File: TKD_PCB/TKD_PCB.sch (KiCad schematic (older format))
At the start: 33 parts, among them U1 ESP32-WROOM-32D

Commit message: Second revision with battery protection circuit attempt
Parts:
- added C? (x3): 0.1uF, symbol Device:C_Small
- added D? (x3): D, symbol Device:D
- added IC?: R5460N208AA-TR-FE, SOT95P280X140-6N, symbol SamacSys_Parts:R5460N233AF-TR-FE
- added Q? (x2): CSD17484F4T, CSD17484F4T, symbol SamacSys_Parts:CSD17484F4T
- added R?: 1k, symbol Device:R
- added R? (x2): 330R, symbol Device:R
- J?: symbol Connector:USB_B_Micro -> TKD_PCB-rescue:USB_B_Micro-Connector
- U?: symbol SamacSys_Parts:1049 -> TKD_PCB-rescue:1049-SamacSys_Parts
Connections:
- net labels added: Batt_1_+, Batt_1_GND, Batt_2_+, Batt_2_GND, Batt_Serie_Connection
- net labels removed: USB_5V_VCC
- wire segments 134 -> 191
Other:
- note added: "Battery Holder for dual 18650"
- note added: "Battery protection circuit"
- note added: "Pad 1 till 6 are screw/attachment pins\nPad 6 = Battery 2 GND\nPad 7 = Battery 1 +\nPad 8 = Battery 2 +\nPad 9 = Battery 1 GND"
- moved on the sheet: C?, D?, R?, SW?, U?

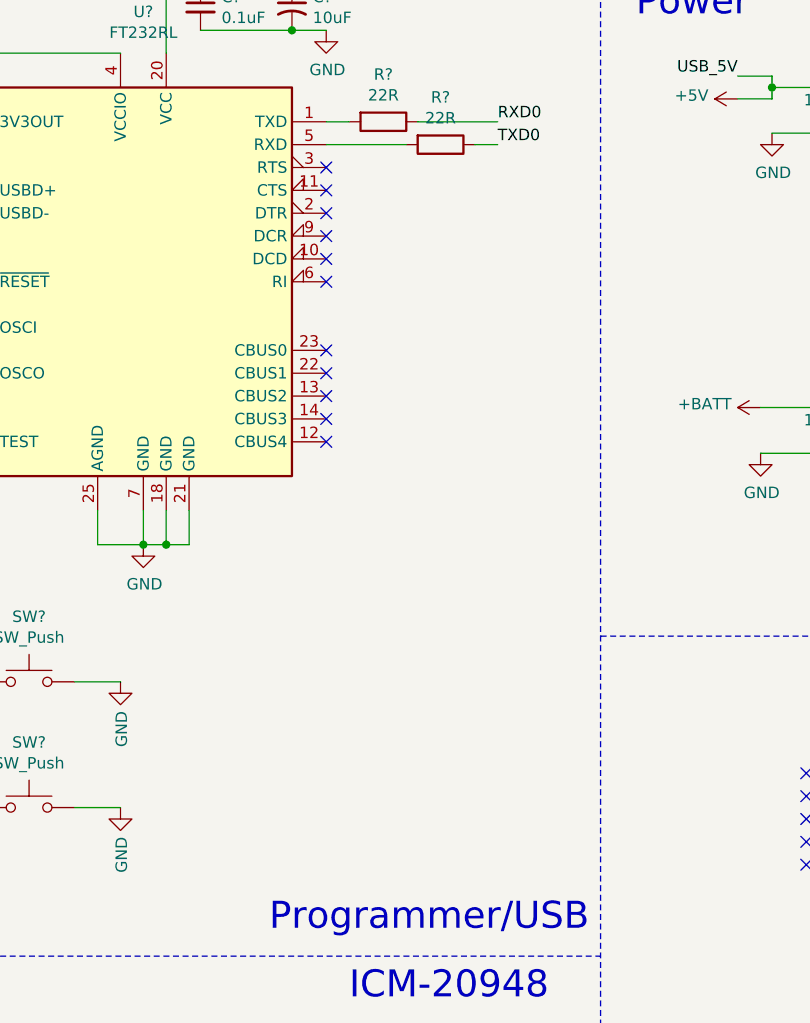
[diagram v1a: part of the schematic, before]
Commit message: Auto programming circuit added
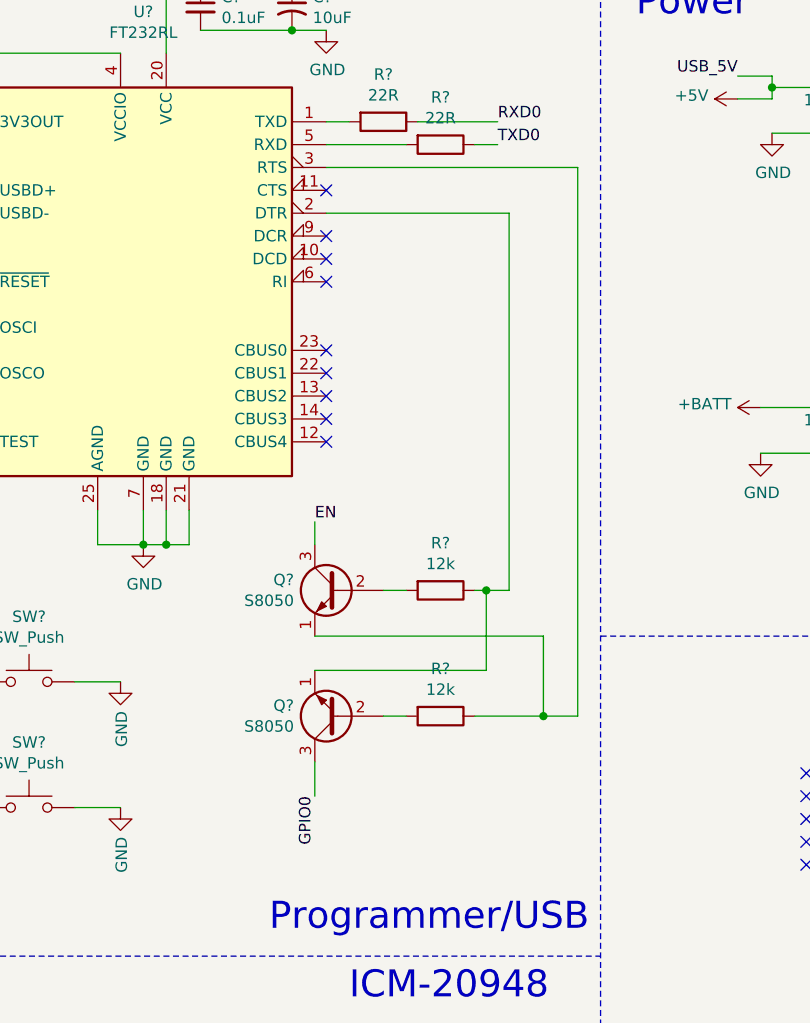
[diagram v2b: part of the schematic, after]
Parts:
- added Q? (x2): S8050, Package_TO_SOT_THT:TO-92_Inline, symbol Transistor_BJT:S8050
- added R? (x2): 12k, symbol Device:R
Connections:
- wire segments 191 -> 207
- no-connect marks 20 -> 18
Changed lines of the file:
@@
 	1    0    0    -1
 $EndComp
-NoConn ~ 6050 1350
 NoConn ~ 6050 1450
-NoConn ~ 6050 1550
 NoConn ~ 6050 1650
 NoConn ~ 6050 1750
@@
 Text Notes 11500 3900 0    50   ~ 0
 Battery protection circuit
+$Comp
+L Transistor_BJT:S8050 Q?
+U 1 1 60276841
+P 6100 3750
+F 0 "Q?" H 6291 3704 50  0000 L CNN
+F 1 "S8050" H 6291 3795 50  0000 L CNN
+F 2 "Package_TO_SOT_THT:TO-92_Inline" H 6300 3675 50  0001 L CIN
+F 3 "http://www.unisonic.com.tw/datasheet/S8050.pdf" H 6100 3750 50  0001 L CNN
+	1    6100 3750
+	-1   0    0    1
+$EndComp
+$Comp
+L Transistor_BJT:S8050 Q?
+U 1 1 602739FF
+P 6100 3200
+F 0 "Q?" H 6291 3246 50  0000 L CNN
+F 1 "S8050" H 6291 3155 50  0000 L CNN
+F 2 "Package_TO_SOT_THT:TO-92_Inline" H 6300 3125 50  0001 L CIN
+F 3 "http://www.unisonic.com.tw/datasheet/S8050.pdf" H 6100 3200 50  0001 L CNN
+	1    6100 3200
+	-1   0    0    -1
+$EndComp
+Text Label 6000 4100 3    50   ~ 0
+GPIO0
+Wire Wire Line
+	6000 3950 6000 4100
+$Comp
+L Device:R R?
+U 1 1 6029CDCC
+P 6550 3750
+F 0 "R?" V 6343 3750 50  0000 C CNN
+F 1 "12k" V 6434 3750 50  0000 C CNN
+F 2 "" V 6480 3750 50  0001 C CNN
+F 3 "~" H 6550 3750 50  0001 C CNN
+	1    6550 3750
+	0    1    1    0
+$EndComp
+$Comp
+L Device:R R?
+U 1 1 6029DF5F
+P 6550 3200
+F 0 "R?" V 6343 3200 50  0000 C CNN
+F 1 "12k" V 6434 3200 50  0000 C CNN
+F 2 "" V 6480 3200 50  0001 C CNN
+F 3 "~" H 6550 3200 50  0001 C CNN
+	1    6550 3200
+	0    1    1    0
+$EndComp
+Text Label 6000 2900 0    50   ~ 0
+EN
+Wire Wire Line
+	6000 3000 6000 2900
+Wire Wire Line
+	6300 3750 6400 3750
+Wire Wire Line
+	6300 3200 6400 3200
+Wire Wire Line
+	6700 3750 7000 3750
+Wire Wire Line
+	7150 3750 7150 1350
+Wire Wire Line
+	7150 1350 6050 1350
+Wire Wire Line
+	6700 3200 6750 3200
+Wire Wire Line
+	6850 3200 6850 1550
+Wire Wire Line
+	6850 1550 6050 1550
+Wire Wire Line
+	6000 3400 7000 3400
+Wire Wire Line
+	7000 3400 7000 3750
+Connection ~ 7000 3750
+Wire Wire Line
+	7000 3750 7150 3750
+Wire Wire Line
+	6000 3550 6750 3550
+Wire Wire Line
+	6750 3550 6750 3200
+Connection ~ 6750 3200
+Wire Wire Line
+	6750 3200 6850 3200
 $EndSCHEMATC

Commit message: Begin of the final assembly
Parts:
- removed IC?: R5460N208AA-TR-FE, SOT95P280X140-6N, symbol SamacSys_Parts:R5460N233AF-TR-FE
- removed Q? (x2): CSD17484F4T, CSD17484F4T, symbol SamacSys_Parts:CSD17484F4T
- added IC1: R5460N233AF-TR-FE, SOT95P280X140-6N, symbol SamacSys_Parts:R5460N233AF-TR-FE
- added Q3, Q4: ZXMN6A09GQTA, SOT230P700X165-4N, symbol SamacSys_Parts:ZXMN6A09GQTA
- C1, C10, C11, C12, C13, C2, C3, C4, C5, C6, C7, C8, C9: renamed from C?; footprint (none) -> Capacitor_SMD:C_0805_2012Metric
- D1, D3, D5, D6: renamed from D?; footprint (none) -> Diode_SMD:D_SOD-123
- J1: renamed from J?; footprint (none) -> Connector_PinSocket_2.54mm:PinSocket_1x07_P2.54mm_Vertical
- J2: renamed from J?; footprint (none) -> Connector_PinSocket_2.54mm:PinSocket_1x08_P2.54mm_Vertical
- J4: renamed from J?; footprint (none) -> Connector_PinHeader_2.54mm:PinHeader_2x02_P2.54mm_Vertical
- J5: renamed from J?; footprint (none) -> Connector_JST:JST_PH_S6B-PH-K_1x06_P2.00mm_Horizontal
- R1, R10, R11, R12, R2, R3, R4, R5, R6, R7, R8, R9: renamed from R?; footprint (none) -> Resistor_SMD:R_0805_2012Metric
- gave numbers to parts that had none: 12
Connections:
- wire segments 207 -> 223
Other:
- moved on the sheet: C11, C12, C13, R10, R11, R12

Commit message: did Remco's homework
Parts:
- C1, C13: value 0.1uF -> 100nF; footprint Capacitor_SMD:C_0805_2012Metric -> Capacitor_SMD:C_0805_2012Metric_Pad1.15x1.40mm_HandSolder; LCSC (none) -> C354369
- C10: renamed from C7; value 0.1uF -> 100nF; footprint Capacitor_SMD:C_0805_2012Metric -> Capacitor_SMD:C_0805_2012Metric_Pad1.15x1.40mm_HandSolder; LCSC (none) -> C354369
- C11: renamed from C9; footprint Capacitor_SMD:C_0805_2012Metric -> Capacitor_SMD:C_0805_2012Metric_Pad1.15x1.40mm_HandSolder; LCSC (none) -> C97916
- C12: renamed from C11; value 0.1uF -> 100nF; footprint Capacitor_SMD:C_0805_2012Metric -> Capacitor_SMD:C_0805_2012Metric_Pad1.15x1.40mm_HandSolder; LCSC (none) -> C354369
- C2, C3: footprint Capacitor_SMD:C_0805_2012Metric -> Capacitor_SMD:C_0805_2012Metric_Pad1.15x1.40mm_HandSolder; LCSC (none) -> C97916
- C4: renamed from C5; value 0.1uF -> 100nF; footprint Capacitor_SMD:C_0805_2012Metric -> Capacitor_SMD:C_0805_2012Metric_Pad1.15x1.40mm_HandSolder; LCSC (none) -> C354369
- C5: renamed from C8; value 0.1uF -> 100nF; footprint Capacitor_SMD:C_0805_2012Metric -> Capacitor_SMD:C_0805_2012Metric_Pad1.15x1.40mm_HandSolder; LCSC (none) -> C354369
- C6: renamed from C10; footprint Capacitor_SMD:C_0805_2012Metric -> Capacitor_SMD:C_0805_2012Metric_Pad1.15x1.40mm_HandSolder; LCSC (none) -> C97916
- C7: renamed from C12; value 0.1uF -> 100nF; footprint Capacitor_SMD:C_0805_2012Metric -> Capacitor_SMD:C_0805_2012Metric_Pad1.15x1.40mm_HandSolder; LCSC (none) -> C354369
- C8: renamed from C4; footprint Capacitor_SMD:C_0805_2012Metric -> Capacitor_SMD:C_0805_2012Metric_Pad1.15x1.40mm_HandSolder; LCSC (none) -> C97916
- C9: renamed from C6; value 0.1uF -> 100nF; footprint Capacitor_SMD:C_0805_2012Metric -> Capacitor_SMD:C_0805_2012Metric_Pad1.15x1.40mm_HandSolder; LCSC (none) -> C354369
- D1: renamed from D5; footprint Diode_SMD:D_SOD-123 -> Diode_SMD:D_0805_2012Metric_Pad1.15x1.40mm_HandSolder
- D2: renamed from D1; LCSC (none) -> C151892
- D3: renamed from D4; footprint (none) -> Diode_SMD:D_0805_2012Metric_Pad1.15x1.40mm_HandSolder
- D4: renamed from D6; footprint Diode_SMD:D_SOD-123 -> Diode_SMD:D_0805_2012Metric_Pad1.15x1.40mm_HandSolder
- D5: renamed from D2; footprint (none) -> Diode_SMD:D_0805_2012Metric_Pad1.15x1.40mm_HandSolder
- D6: renamed from D3; footprint Diode_SMD:D_SOD-123 -> Diode_SMD:D_0805_2012Metric_Pad1.15x1.40mm_HandSolder; LCSC (none) -> C72036
- IC1: footprint SOT95P280X140-6N -> SamacSys_Parts:SOT95P280X140-6N; symbol SamacSys_Parts:R5460N233AF-TR-FE -> TKD_PCB-rescue:R5460N233AF-TR-FE-SamacSys_Parts
- J1: renamed from J3; LCSC (none) -> C46396
- J2: renamed from J5; footprint Connector_JST:JST_PH_S6B-PH-K_1x06_P2.00mm_Horizontal -> Connector_PinSocket_2.54mm:PinSocket_1x06_P2.54mm_Vertical
- J4: renamed from J1; Mouser Part Number (none) -> 848-R5460N233AFTRFE
- Q1: renamed from Q3; footprint SOT230P700X165-4N -> SamacSys_Parts:SOT230P700X165-4N; symbol SamacSys_Parts:ZXMN6A09GQTA -> TKD_PCB-rescue:ZXMN6A09GQTA-SamacSys_Parts
- Q2: renamed from Q4; footprint SOT230P700X165-4N -> SamacSys_Parts:SOT230P700X165-4N; symbol SamacSys_Parts:ZXMN6A09GQTA -> TKD_PCB-rescue:ZXMN6A09GQTA-SamacSys_Parts
- Q3: renamed from Q1; Mouser Part Number (none) -> 512-SS8050DTA
- Q4: renamed from Q2; Mouser Part Number (none) -> 512-SS8050DTA
- R1: renamed from R4; footprint Resistor_SMD:R_0805_2012Metric -> Resistor_SMD:R_0805_2012Metric_Pad1.15x1.40mm_HandSolder; Mouser Part Number (none) -> 71-RCA080522R0FKEA
- R10: renamed from R7; footprint Resistor_SMD:R_0805_2012Metric -> Resistor_SMD:R_0805_2012Metric_Pad1.15x1.40mm_HandSolder; Mouser Part Number (none) -> 71-CRCW080512K0JNEA
- R11: renamed from R3; footprint Resistor_SMD:R_0805_2012Metric -> Resistor_SMD:R_0805_2012Metric_Pad1.15x1.40mm_HandSolder; Mouser Part Number (none) -> 71-CRCW080510K0FKEAC
- R12: renamed from R1; footprint Resistor_SMD:R_0805_2012Metric -> Resistor_SMD:R_0805_2012Metric_Pad1.15x1.40mm_HandSolder; Mouser Part Number (none) -> 71-CRCW0805J-5K
- R2: renamed from R9; value 330R -> 1k; footprint Resistor_SMD:R_0805_2012Metric -> Resistor_SMD:R_0805_2012Metric_Pad1.15x1.40mm_HandSolder; Mouser Part Number (none) -> 71-CRCW08051K00JNEAC
- R3: renamed from R5; footprint Resistor_SMD:R_0805_2012Metric -> Resistor_SMD:R_0805_2012Metric_Pad1.15x1.40mm_HandSolder; Mouser Part Number (none) -> 71-RCA080522R0FKEA
- R4: renamed from R11; footprint Resistor_SMD:R_0805_2012Metric -> Resistor_SMD:R_0805_2012Metric_Pad1.15x1.40mm_HandSolder; Mouser Part Number (none) -> 71-CRCW0805330RFKEAC
- R5: renamed from R10; footprint Resistor_SMD:R_0805_2012Metric -> Resistor_SMD:R_0805_2012Metric_Pad1.15x1.40mm_HandSolder; Mouser Part Number (none) -> 71-CRCW08051K00JNEAC
- R6: renamed from R12; footprint Resistor_SMD:R_0805_2012Metric -> Resistor_SMD:R_0805_2012Metric_Pad1.15x1.40mm_HandSolder; Mouser Part Number (none) -> 71-CRCW0805330RFKEAC
- R7: renamed from R8; value 330R -> 1k; footprint Resistor_SMD:R_0805_2012Metric -> Resistor_SMD:R_0805_2012Metric_Pad1.15x1.40mm_HandSolder; Mouser Part Number (none) -> 71-CRCW08051K00JNEAC
- R8: renamed from R6; footprint Resistor_SMD:R_0805_2012Metric -> Resistor_SMD:R_0805_2012Metric_Pad1.15x1.40mm_HandSolder; Mouser Part Number (none) -> 71-CRCW080512K0JNEA
- R9: renamed from R2; footprint Resistor_SMD:R_0805_2012Metric -> Resistor_SMD:R_0805_2012Metric_Pad1.15x1.40mm_HandSolder; Mouser Part Number (none) -> 71-CRCW080510K0FKEAC
- SW1, SW2: footprint (none) -> Button_Switch_THT:SW_PUSH_6mm; Mouser Part Number (none) -> 612-LL3301NF065QG
- SW3: footprint (none) -> SamacSys_Parts:AYZ0103AGRLC; Mouser Part Number (none) -> 611-AYZ0103AGRLC
- U1: renamed from U5; Height (none) -> (none); LCSC (none) -> C351784
- U2: Mouser Part Number (none) -> 895-FT232RL
- U3: renamed from U4; footprint (none) -> Package_TO_SOT_SMD:TO-263-3_TabPin4; LCSC (none) -> (none); Mouser Part Number (none) -> 926-LM1085IS50NOPB
- U4: renamed from U1; LCSC (none) -> C473012; Mouser Part Number (none) -> 356-ES32WROOM32D16MB
- U5: renamed from U3; footprint 1049 -> SamacSys_Parts:1049
- renumbered J4 to J3, J2 to J5
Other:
- moved on the sheet: J5

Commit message: some more routing
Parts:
- removed J1: USB_B_Micro, symbol TKD_PCB-rescue:USB_B_Micro-Connector
- added J1: USB2066-05-RBHM-15-STB-00-00-A, USB206605RBHM15STB0000A, symbol SamacSys_Parts:USB2066-05-RBHM-15-STB-00-00-A
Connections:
- net GND: now also J1.5, J1.MP1, J1.MP2, J1.MP3, J1.MP4
- net at D2.2 (A): now also J1.1
- net at U2.16 (USBD-): now also J1.2
- net at U2.15 (USBD+): now also J1.3
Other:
- moved on the sheet: D2
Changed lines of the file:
@@
-	1    0    0    -1
-$EndComp
-$Comp
-L TKD_PCB-rescue:USB_B_Micro-Connector J1
-U 1 1 5F3F2222
-P 3700 1450
-F 0 "J1" H 3757 1917 50  0000 C CNN
-F 1 "USB_B_Micro" H 3757 1826 50  0000 C CNN
-F 2 "" H 3850 1400 50  0001 C CNN
-F 3 "~" H 3850 1400 50  0001 C CNN
-F 4 "C46396" H 3700 1450 50  0001 C CNN "LCSC"
-	1    3700 1450
 	1    0    0    -1
 $EndComp
@@
 L power:GND #PWR09
 U 1 1 5F408DD7
-P 3700 2000
-F 0 "#PWR09" H 3700 1750 50  0001 C CNN
-F 1 "GND" H 3705 1827 50  0000 C CNN
-F 2 "" H 3700 2000 50  0001 C CNN
-F 3 "" H 3700 2000 50  0001 C CNN
-	1    3700 2000
-	1    0    0    -1
-$EndComp
-Wire Wire Line
-	3700 1850 3700 2000
-Wire Wire Line
-	4000 1450 4450 1450
-Wire Wire Line
-	4000 1550 4450 1550
-Text Label 4200 900  1    50   ~ 0
+P 4050 1150
+F 0 "#PWR09" H 4050 900 50  0001 C CNN
+F 1 "GND" H 4055 977 50  0000 C CNN
+F 2 "" H 4050 1150 50  0001 C CNN
+F 3 "" H 4050 1150 50  0001 C CNN
+	1    4050 1150
+	0    -1   -1   0
+$EndComp
+Wire Wire Line
+	3900 1150 4050 1150
+Text Label 4000 2000 2    50   ~ 0
 USB_5V
 Wire Wire Line
@@
 L Device:D D2
 U 1 1 5F4EC909
-P 4200 1100
-F 0 "D2" V 4154 1180 50  0000 L CNN
-F 1 "D" V 4245 1180 50  0000 L CNN
-F 2 "Diode_SMD:D_SOD-123" H 4200 1100 50  0001 C CNN
-F 3 "~" H 4200 1100 50  0001 C CNN
-F 4 "C151892" V 4200 1100 50  0001 C CNN "LCSC"
-	1    4200 1100
-	0    1    1    0
-$EndComp
-Wire Wire Line
-	4200 950  4200 900
+P 4050 1850
+F 0 "D2" V 4004 1930 50  0000 L CNN
+F 1 "D" V 4095 1930 50  0000 L CNN
+F 2 "Diode_SMD:D_SOD-123" H 4050 1850 50  0001 C CNN
+F 3 "~" H 4050 1850 50  0001 C CNN
+F 4 "C151892" V 4050 1850 50  0001 C CNN "LCSC"
+	1    4050 1850
+	0    -1   -1   0
+$EndComp
+Wire Wire Line
+	4050 2000 4000 2000
 Wire Wire Line
 	9200 1300 9200 1400
@@
 Connection ~ 9900 2600
 Connection ~ 10250 3150
-Wire Wire Line
-	4000 1250 4200 1250
 $Comp
 L Device:D D6
@@
 Wire Notes Line
 	7250 3400 11400 3400
+$Comp
+L SamacSys_Parts:USB2066-05-RBHM-15-STB-00-00-A J1
+U 1 1 60DB3BDD
+P 3900 1550
+F 0 "J1" H 4350 1815 50  0000 C CNN
+F 1 "USB2066-05-RBHM-15-STB-00-00-A" H 4350 1724 50  0000 C CNN
+F 2 "USB206605RBHM15STB0000A" H 4650 1650 50  0001 L CNN
+F 3 "" H 4650 1550 50  0001 L CNN
+F 4 "GCT (GLOBAL CONNECTOR TECHNOLOGY) - USB2066-05-RBHM-15-STB-00-00-A - USB Connector, Mini USB Type B, USB 2.0, Receptacle, 5 Positions, Surface Mount, Right Angle" H 4650 1450 50  0001 L CNN "Description"
+F 5 "4.25" H 4650 1350 50  0001 L CNN "Height"
+F 6 "640-2665RBHM15STB00A" H 4650 1250 50  0001 L CNN "Mouser Part Number"
+F 7 "https://www.mouser.co.uk/ProductDetail/GCT/USB2066-05-RBHM-15-STB-00-00-A?qs=KUoIvG%2F9IlZEo87a0wQR%252BA%3D%3D" H 4650 1150 50  0001 L CNN "Mouser Price/Stock"
+F 8 "GCT (GLOBAL CONNECTOR TECHNOLOGY)" H 4650 1050 50  0001 L CNN "Manufacturer_Name"
+F 9 "USB2066-05-RBHM-15-STB-00-00-A" H 4650 950 50  0001 L CNN "Manufacturer_Part_Number"
+	1    3900 1550
+	-1   0    0    1
+$EndComp
+Wire Wire Line
+	4050 1700 4050 1550
+Wire Wire Line
+	4050 1550 3900 1550
+Wire Wire Line
+	3900 1450 4200 1450
+Wire Wire Line
+	4200 1450 4200 1550
+Wire Wire Line
+	4200 1550 4450 1550
+Wire Wire Line
+	3900 1350 4250 1350
+Wire Wire Line
+	4250 1350 4250 1450
+Wire Wire Line
+	4250 1450 4450 1450
+$Comp
+L power:GND #PWR0101
+U 1 1 60E36373
+P 3000 1250
+F 0 "#PWR0101" H 3000 1000 50  0001 C CNN
+F 1 "GND" H 3005 1077 50  0000 C CNN
+F 2 "" H 3000 1250 50  0001 C CNN
+F 3 "" H 3000 1250 50  0001 C CNN
+	1    3000 1250
+	0    1    1    0
+$EndComp
+Wire Wire Line
+	3000 1250 3000 1350
+Connection ~ 3000 1250
+Wire Wire Line
+	3000 1350 3000 1450
+Connection ~ 3000 1350
+Wire Wire Line
+	3000 1450 3000 1550
+Connection ~ 3000 1450
 $EndSCHEMATC
